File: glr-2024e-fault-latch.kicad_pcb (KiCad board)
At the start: 2 copper layers, 110 x 90 mm, 108 parts, among them K101 Fujitsu_FTR-LYAA005x, K102 Fujitsu_FTR-LYAA005x, K103 Fujitsu_FTR-LYAA005x, Q101 Q_NPN_BEC, Q102 Q_NPN_BEC, Q103 Q_NPN_BEC, Q104 Q_NPN_BEC, Q105 Q_NMOS_GSD, Q106 Q_NMOS_GSD, Q107 Q_PMOS_GSD, Q108 Q_PMOS_GSD, Q109 Q_NMOS_GDS, Q110 Q_NPN_BEC, Q111 Q_NPN_BEC, Q112 Q_NMOS_GSD, Q113 Q_PMOS_GSD, SW101 SW_Omron_B3FS, SW102 SW_Omron_B3FS, SW103 SW_Omron_B3FS, U101 SFH617A-1, U102 SFH617A-1, U103 SFH617A-1, U104 74AHC1G00, U105 74AHC1G00, U106 74AHC1G00, U107 74LS279, U108 641964-1, U109 SFH617A-1, U110 SFH617A-1, U111 641964-1, U112 641964-1, U113 641964-1, U114 641964-1, U115 641964-1, U116 641964-1, U117 74AHC1G00, U118 LM555xM, U119 74AHC1G00, U120 641964-1, U121 SFH617A-1, U122 641964-1

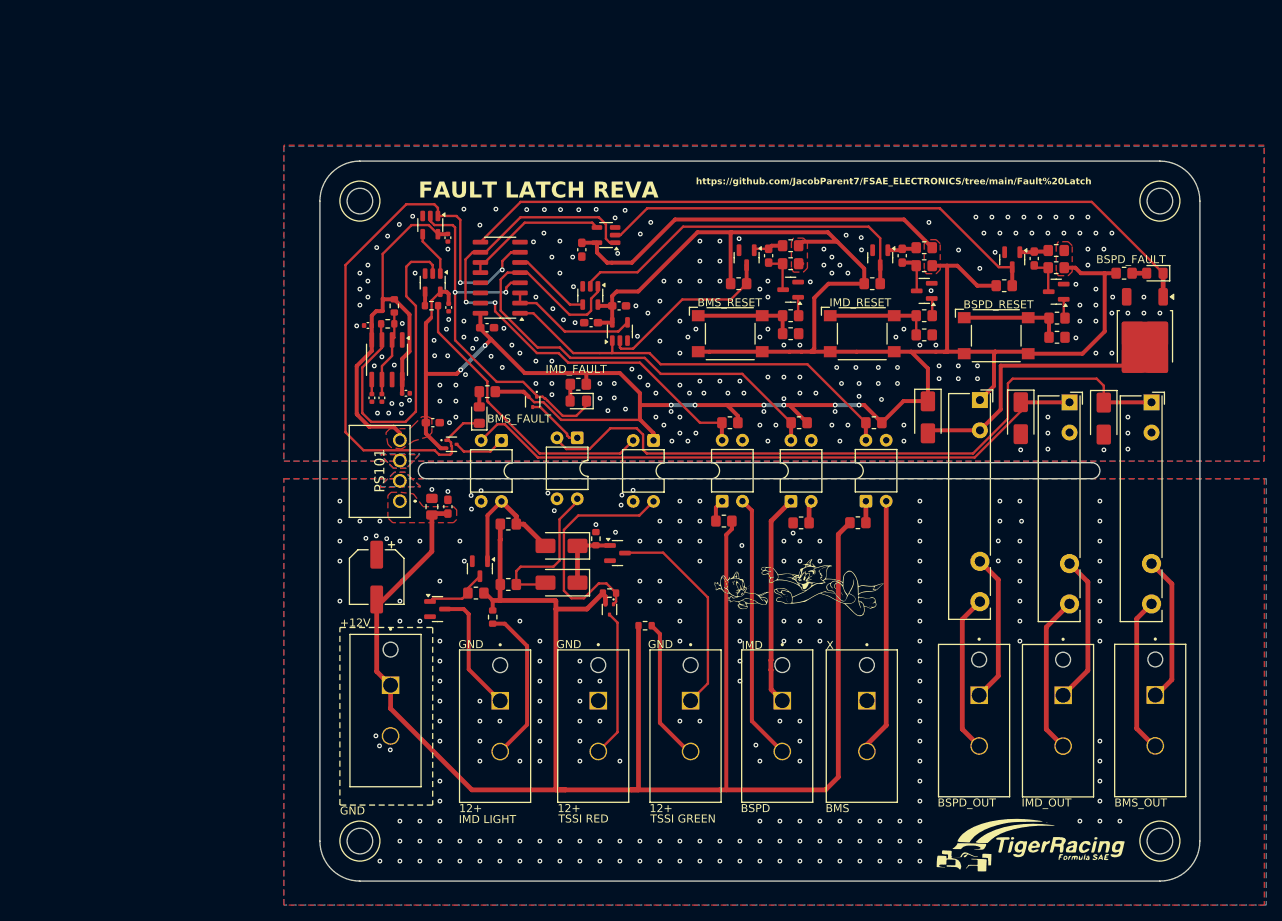
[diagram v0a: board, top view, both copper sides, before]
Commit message: work in progress
keep only bms and imd
remove tssi stuff

Co-Authored-By: wallalex0 <97884125+wallalex0@users.noreply.github.com>
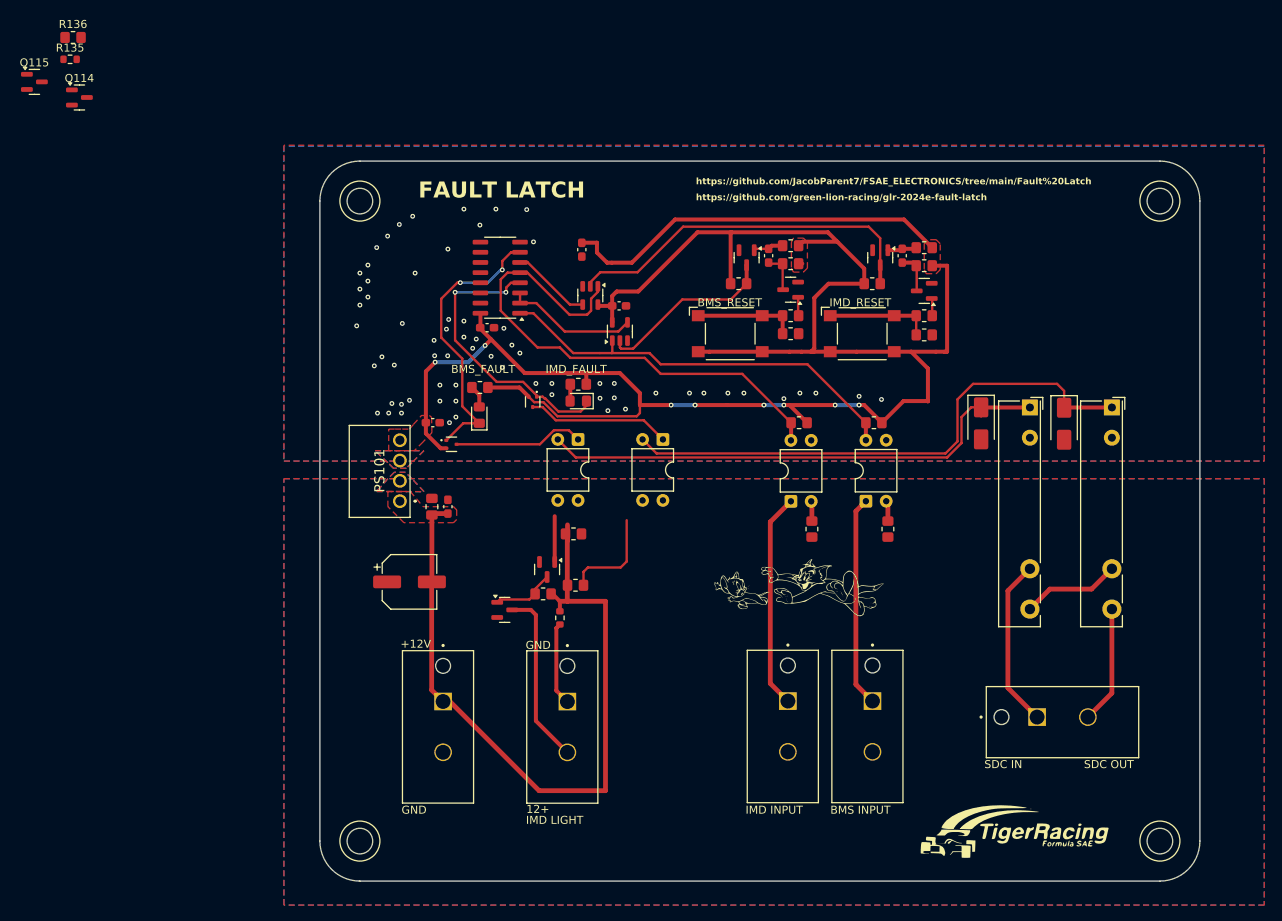
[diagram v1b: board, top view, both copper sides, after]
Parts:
- removed C104: 100n, Capacitor_SMD:C_0603_1608Metric_Pad1.08x0.95mm_HandSolder
- removed C106: 10n, Capacitor_SMD:C_0603_1608Metric_Pad1.08x0.95mm_HandSolder
- removed C107: 1u, Capacitor_SMD:C_0402_1005Metric
- removed C108, C110, C112: 0.1u, Capacitor_SMD:C_0402_1005Metric
- removed C109: .01u, Capacitor_SMD:C_0402_1005Metric
- removed C111: 22u, Capacitor_SMD:C_0402_1005Metric
- removed D103: RED, LED_SMD:LED_0805_2012Metric_Pad1.15x1.40mm_HandSolder
- removed D105, D107, D108: D_Schottky, Diode_SMD:D_SMA
- removed K102: Fujitsu_FTR-LYAA005x, Relay_THT:Relay_SPST-NO_Fujitsu_FTR-LYAA005x_FormA_Vertical
- removed Q109: Q_NMOS_GDS, Package_TO_SOT_SMD:TO-252-2
- removed Q110, Q111: Q_NPN_BEC, Package_TO_SOT_SMD:SOT-23
- removed Q112: Q_NMOS_GSD, Package_TO_SOT_SMD:SOT-23
- removed Q113: Q_PMOS_GSD, Package_TO_SOT_SMD:SOT-523
- removed R104, R107, R123: 10k, Resistor_SMD:R_0805_2012Metric_Pad1.20x1.40mm_HandSolder
- removed R118: 270R, Resistor_SMD:R_0805_2012Metric_Pad1.20x1.40mm_HandSolder
- removed R122, R127: 100k, Resistor_SMD:R_0805_2012Metric_Pad1.20x1.40mm_HandSolder
- removed R124, R129: 1k, Resistor_SMD:R_0805_2012Metric_Pad1.20x1.40mm_HandSolder
- removed R128, R133, R134: 10k, Resistor_SMD:R_0603_1608Metric
- removed R130: 270R, Resistor_SMD:R_0603_1608Metric
- removed R131: 15k, Resistor_SMD:R_0603_1608Metric
- removed R132: 100k, Resistor_SMD:R_0603_1608Metric
- removed SW103: SW_Omron_B3FS, Button_Switch_SMD:SW_SPST_Omron_B3FS-100xP
- removed U103, U121: SFH617A-1, Package_DIP:DIP-4_W7.62mm
- removed U106, U117, U119: 74AHC1G00, Package_TO_SOT_SMD:SOT-23-5
- removed U111, U113, U114, U122: 641964-1, 641964-1:TE_641964-1
- removed U118: LM555xM, Package_SO:SOIC-8_3.9x4.9mm_P1.27mm
- added Q114: Q_NMOS_GSD, Package_TO_SOT_SMD:SOT-23, F.Cu at (39.2, 36.1)
- added Q115: Q_NMOS_GSD, Package_TO_SOT_SMD:SOT-23, F.Cu at (33.5, 34.2)
- added R135: 510R, Resistor_SMD:R_0603_1608Metric, F.Cu at (38.0, 31.4)
- added R136: 10k, Resistor_SMD:R_0805_2012Metric_Pad1.20x1.40mm_HandSolder, F.Cu at (38.4, 28.6)
- R112: value 500R -> 510R
- moved U109 10.7 mm to (112.1, 78.9)
- moved U110 9.58 mm to (101.5, 78.9)
- moved Q105 8.40 mm to (97.6, 95.1)
- moved Q106 8.40 mm to (92.3, 100.2)
- moved R121 8.40 mm to (97.1, 98.2)
- moved R112 8.40 mm to (99.2, 101.2)
- moved R125 8.40 mm to (101.2, 97.1)
- moved U108 8.40 mm to (100.2, 111.6)
- moved R126 8.24 mm to (100.9, 90.7)
- moved U120 6.87 mm to (84.6, 111.6)
- moved D104 5.00 mm to (162.2, 76.9)
- moved D106 5.00 mm to (151.9, 76.9)
- moved K101 5.00 mm to (168.2, 74.9)
- moved K103 5.00 mm to (158.0, 74.9)
- moved U112 4.24 mm to (158.9, 113.6), turned to 0 degrees
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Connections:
- net /IMD_HV renamed /IMD_INPUT
- net Net-(K103-Pad13) renamed /SDC_IN
- K101 pad 13: Net-(K101-Pad13) -> /SDC
- K101 pad 14: Net-(K101-Pad14) -> /SDC_OUT
- K103 pad 14: Net-(K103-Pad14) -> /SDC
- R102 pad 1: Net-(R102-Pad1) -> GNDPWR
- R102 pad 2: +12V -> Net-(R102-Pad2)
- U101 pad 1: Net-(R102-Pad1) -> /BMS_INPUT
- U101 pad 2: /NBMS_HV -> Net-(R102-Pad2)
- U107 pad 10: /NBPSD_LV -> unconnected-(U107C-~{R}-Pad10)
- U107 pad 11: Net-(U106-Pad4) -> unconnected-(U107C-~{S}-Pad11)
- U107 pad 12: Net-(U106-Pad4) -> unconnected-(U107C-~{S}-Pad12)
- U107 pad 9: Net-(D103-K) -> unconnected-(U107C-Q-Pad9)
- U108 pad 1: Net-(Q106-D) -> Net-(R112-Pad2)
- U108 pad 2: Net-(R112-Pad2) -> Net-(Q106-D)
- U112 pad 2: Net-(K103-Pad14) -> /SDC_OUT
- U115 pad 1: unconnected-(U115-Pad1) -> /BMS_INPUT
- U115 pad 2: /NBMS_HV -> unconnected-(U115-Pad2)
- U116 pad 2: /BSPD_HV -> unconnected-(U116-Pad2)
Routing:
- net +12V: track 231.8 -> 92.6 mm
- net +5V: track 406.5 -> 281.6 mm
- net Net-(D103-K): track 94.1 -> 0.00 mm
- net /NBPSD_LV: track 69.7 -> 0.00 mm, vias 2 -> 0
- net /NRESET_BSPD: track 56.4 -> 0.00 mm
- net /IMD_SR: track 79.1 -> 35.5 mm
- net /CLOCK: track 43.4 -> 0.00 mm
- net Net-(R133-Pad1): track 36.1 -> 0.00 mm
- net /BSPD_HV: track 33.4 -> 0.00 mm
- net Net-(D105-A): track 33.4 -> 0.00 mm
- net /NBMS_HV: track 31.4 -> 0.00 mm
- net Net-(Q113-G): track 29.9 -> 0.00 mm
- net Net-(Q112-D): track 26.5 -> 0.00 mm
- net /BMS_INPUT: track 0.00 -> 26.4 mm
- net Net-(K103-Pad14): track 19.8 -> 0.00 mm
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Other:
- outline, holes or cut-outs redrawn
- board text added: "BMS INPUT"
- board text added: "FAULT LATCH"
- board text added: "IMD INPUT"
- board text added: "SDC IN"
- board text added: "SDC OUT"
- board text added: "https://github.com/green-lion-racing/glr-2024e-fault-latch"
- board text removed: "BMS"
- board text removed: "BMS_OUT"
- board text removed: "BSPD"
- board text removed: "BSPD_FAULT"
- board text removed: "BSPD_OUT"
- board text removed: "BSPD_RESET"
- board text removed: "FAULT LATCH REVA"
- board text removed: "IMD"
- board text removed: "IMD_OUT"
- board text removed: "TSSI GREEN"
- board text removed: "TSSI RED"
- board text removed: "X"

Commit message: almost finished
add bms light logic
improve overall placements of components
improve routing
improve silk component identifiers

Co-Authored-By: wallalex0 <97884125+wallalex0@users.noreply.github.com>
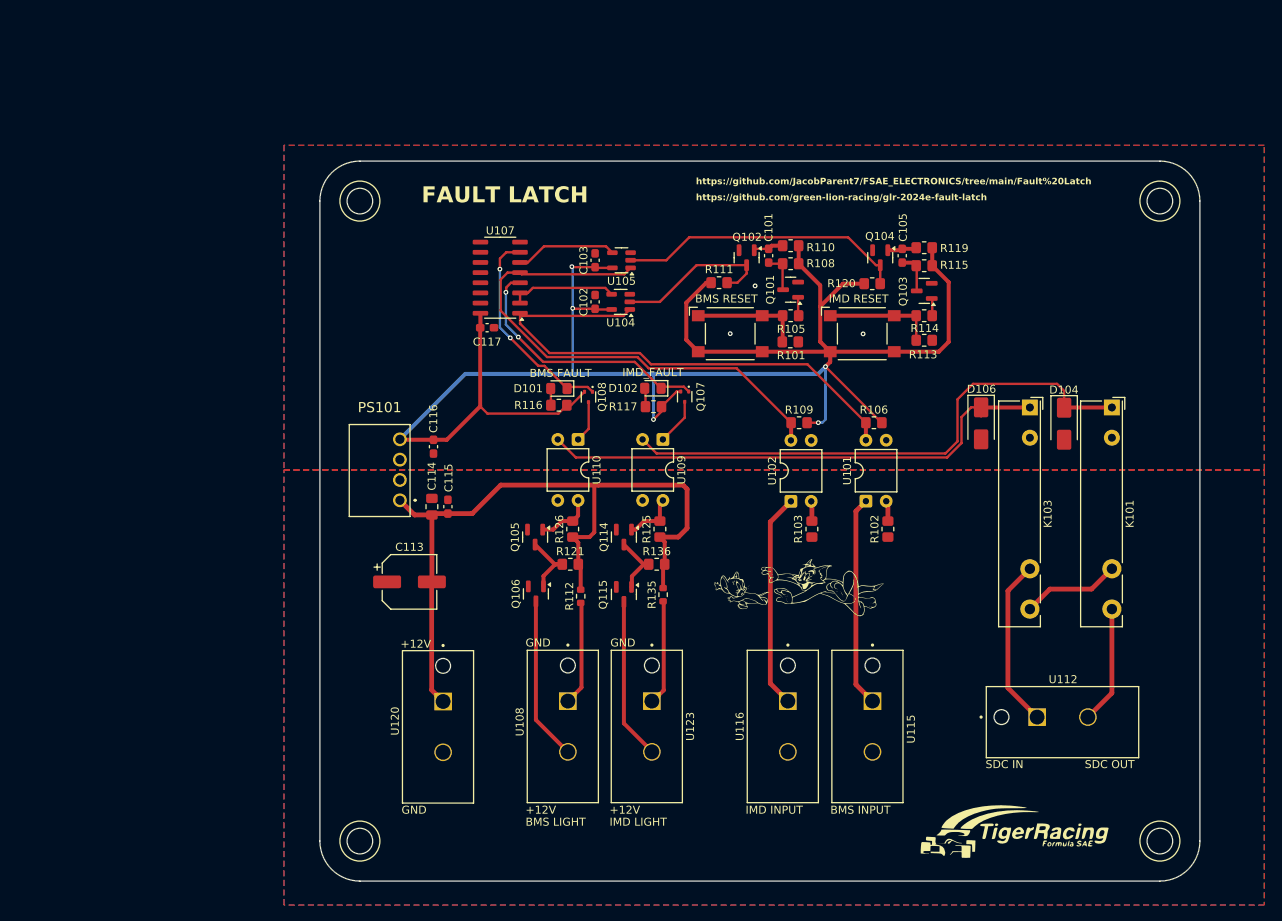
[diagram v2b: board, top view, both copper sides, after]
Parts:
- added U123: 641964-1, 641964-1:TE_641964-1, F.Cu at (110.7, 111.6)
- moved R135 99.9 mm to (112.1, 98.3), turned to -90 degrees
- moved R136 98.3 mm to (111.3, 94.5), turned to 180 degrees
- moved Q115 97.6 mm to (107.2, 98.2), turned to -90 degrees
- moved Q114 87.5 mm to (107.2, 91.1), turned to -90 degrees
- moved Q107 19.0 mm to (114.8, 73.5)
- moved Q108 18.1 mm to (102.8, 73.6), turned to -90 degrees
- moved R125 12.7 mm to (111.7, 90.1), turned to 90 degrees
- moved D101 10.5 mm to (99.1, 72.5), turned to 180 degrees
- moved R116 10.1 mm to (99.1, 74.6)
- moved R117 9.81 mm to (110.9, 74.8)
- moved D102 9.46 mm to (110.8, 72.5)
- moved U105 5.88 mm to (106.9, 56.5), turned to 180 degrees
- moved R121 5.02 mm to (100.5, 94.5)
- moved Q106 4.38 mm to (96.2, 98.2), turned to -90 degrees
- moved Q105 4.32 mm to (96.1, 91.1)
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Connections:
- R125 pad 2: /BMS_Green -> /BMS_GREEN
- U109 pad 4: /BMS_Green -> /BMS_GREEN
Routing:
- net +5V: track 281.6 -> 227.4 mm, vias 8 -> 5
- net Net-(Q115-D): track 0.00 -> 20.2 mm
- net /NBMS_LV: track 52.8 -> 66.1 mm
- net Net-(R135-Pad2): track 0.00 -> 13.2 mm
- net /BMS_Green: track 12.8 -> 0.00 mm
- net Net-(Q107-D): track 18.0 -> 5.82 mm
- net Net-(Q108-D): track 16.4 -> 5.23 mm
- net /NRESET_IMD: track 45.9 -> 36.2 mm
- net /IMD_SR: track 35.5 -> 26.5 mm
- net Net-(Q114-D): track 0.00 -> 8.19 mm
- net /BMS_GREEN: track 0.00 -> 6.73 mm
- net Net-(U104-Pad4): track 16.6 -> 13.3 mm
- net +12V: track 92.6 -> 95.5 mm
- net /BMS_SR: track 36.0 -> 33.1 mm
- net Net-(U107B-~{S}): track 10.0 -> 12.7 mm
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- removed copper zone on F.Cu, net +12V
- removed copper zone on F.Cu, net +5V
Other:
- board text added: "BMS FAULT"
- board text added: "BMS LIGHT"
- board text added: "BMS RESET"
- board text added: "IMD RESET"
- board text added: "{ "ViaStitching": "0.2", "stitch_zone_0": { "HSpacing": "1", "VSpacing": "1", "HOffset": "0", "VOffset": "0", "Clearance": "0", "Randomize": false } }"
- board text removed: "12+"
- board text removed: "BMS_FAULT"
- board text removed: "BMS_RESET"
- board text removed: "IMD_RESET"

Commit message: add details
add license

Co-Authored-By: wallalex0 <97884125+wallalex0@users.noreply.github.com>
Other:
- board text added: "${COMPANY} ${TITLE} ${PROJECTNAME} ${REVISION} ${ISSUE_DATE}"
- board text added: "FAULT LATCH ${REVISION}"
- board text removed: "FAULT LATCH"
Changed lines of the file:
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@@
 	)
 	(paper "A4")
+	(title_block
+		(title "Fault latch for IMD and BMS/AMS")
+		(date "2025-06-13")
+		(rev "v3")
+		(company "Green Lion Racing")
+		(comment 1 "Alexander Wallrodt")
+	)
 	(layers
 		(0 "F.Cu" signal)
@@
 		)
 	)
-	(gr_text "FAULT LATCH"
+	(gr_text "FAULT LATCH ${REVISION}"
 		(at 81.922 49.472 0)
 		(layer "F.SilkS" knockout)
@@
 		)
 	)
+	(gr_text "${COMPANY}\n${TITLE}\n${PROJECTNAME} ${REVISION}\n${ISSUE_DATE}"
+		(at 170.222 62.172 0)
+		(layer "B.SilkS")
+		(effects
+			(font
+				(size 1.5 1.5)
+				(thickness 0.1875)
+			)
+			(justify left bottom mirror)
+		)
+	)
 	(gr_text "{\n  \"ViaStitching\": \"0.2\",\n  \"stitch_zone_0\": {\n    \"HSpacing\": \"1\",\n    \"VSpacing\": \"1\",\n    \"HOffset\": \"0\",\n    \"VOffset\": \"0\",\n    \"Clearance\": \"0\",\n    \"Randomize\": false\n  }\n}"
 		(at 0 0 0)
@@
 	)
 	(segment
-		(start 115.022 61.772)
-		(end 117.522 59.272)
-		(width 0.5)
-		(layer "F.Cu")
-		(net 7)
-	)
-	(segment
 		(start 131.7615 66.649)
 		(end 131.7615 62.249)
@@
 	)
 	(segment
-		(start 134.6105 59.4)
-		(end 137.2625 59.4)
-		(width 0.5)
-		(layer "F.Cu")
-		(net 7)
-	)
-	(segment
 		(start 141.0125 67.9)
 		(end 146.594 67.9)
@@
 	)
 	(segment
+		(start 116.5125 67.9)
+		(end 115.022 66.4095)
+		(width 0.5)
+		(layer "F.Cu")
+		(net 7)
+	)
+	(segment
 		(start 133.0125 69.1815)
 		(end 132.422 69.772)
@@
 	(segment
 		(start 131.7615 59.599)
+		(end 131.9605 59.4)
+		(width 0.5)
+		(layer "F.Cu")
+		(net 7)
+	)
+	(segment
+		(start 131.7615 59.599)
 		(end 129.0625 56.9)
 		(width 0.5)
@@
 	)
 	(segment
-		(start 115.022 66.4095)
-		(end 115.022 61.772)
+		(start 115.022 60.572)
+		(end 116.322 59.272)
 		(width 0.5)
 		(layer "F.Cu")
@@
 	)
 	(segment
-		(start 131.7615 62.249)
-		(end 134.6105 59.4)
+		(start 115.022 66.4095)
+		(end 115.022 60.572)
 		(width 0.5)
 		(layer "F.Cu")
@@
 	)
 	(segment
-		(start 117.522 59.272)
-		(end 118.122 59.272)
-		(width 0.5)
-		(layer "F.Cu")
-		(net 7)
-	)
-	(segment
 		(start 131.5145 76.7795)
 		(end 131.522 76.772)
@@
 	)
 	(segment
-		(start 116.5125 67.9)
-		(end 115.022 66.4095)
-		(width 0.5)
-		(layer "F.Cu")
-		(net 7)
-	)
-	(segment
 		(start 99.039181 75.639114)
 		(end 90.163302 75.639114)
@@
 		(width 0.5)
 		(layer "F.Cu")
+		(net 7)
+	)
+	(segment
+		(start 131.9605 59.4)
+		(end 137.2625 59.4)
+		(width 0.5)
+		(layer "F.Cu")
+		(net 7)
+	)
+	(segment
+		(start 116.322 59.272)
+		(end 118.122 59.272)
+		(width 0.5)
+		(layer "F.Cu")
